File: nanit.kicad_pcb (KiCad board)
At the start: 2 copper layers, 31.2 x 53.3 mm, 66 parts, among them J1 USB_B_Micro, J2 Nokia 2660/2760 mini, Q1 BC857, Q2 IRLML6344, Q4 BC847, SW1 Button 1, SW2 Button 2, U1 LTC4054ES5-4.2, U2 ATmega88PA-AU, Y1 32.768 KHz

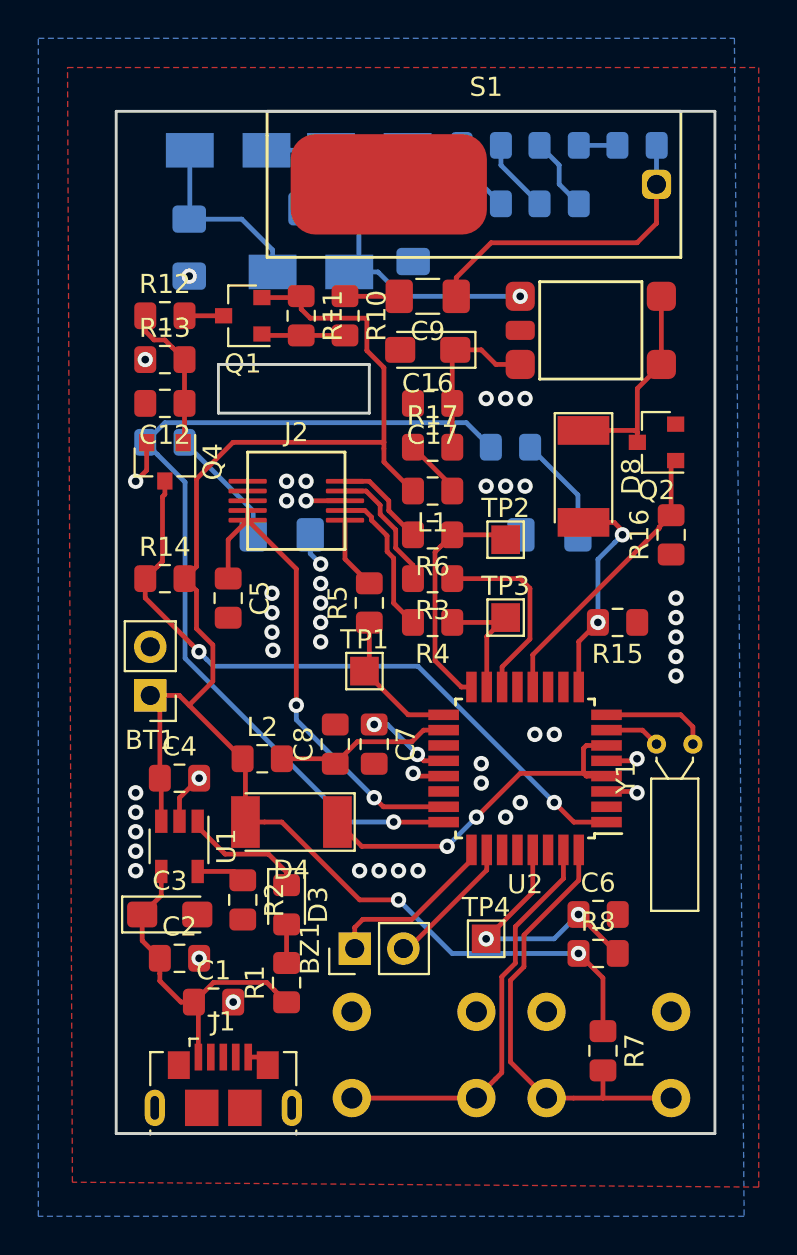
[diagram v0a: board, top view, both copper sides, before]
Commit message: Added LED driver for LCD display, gerbers for rev.A
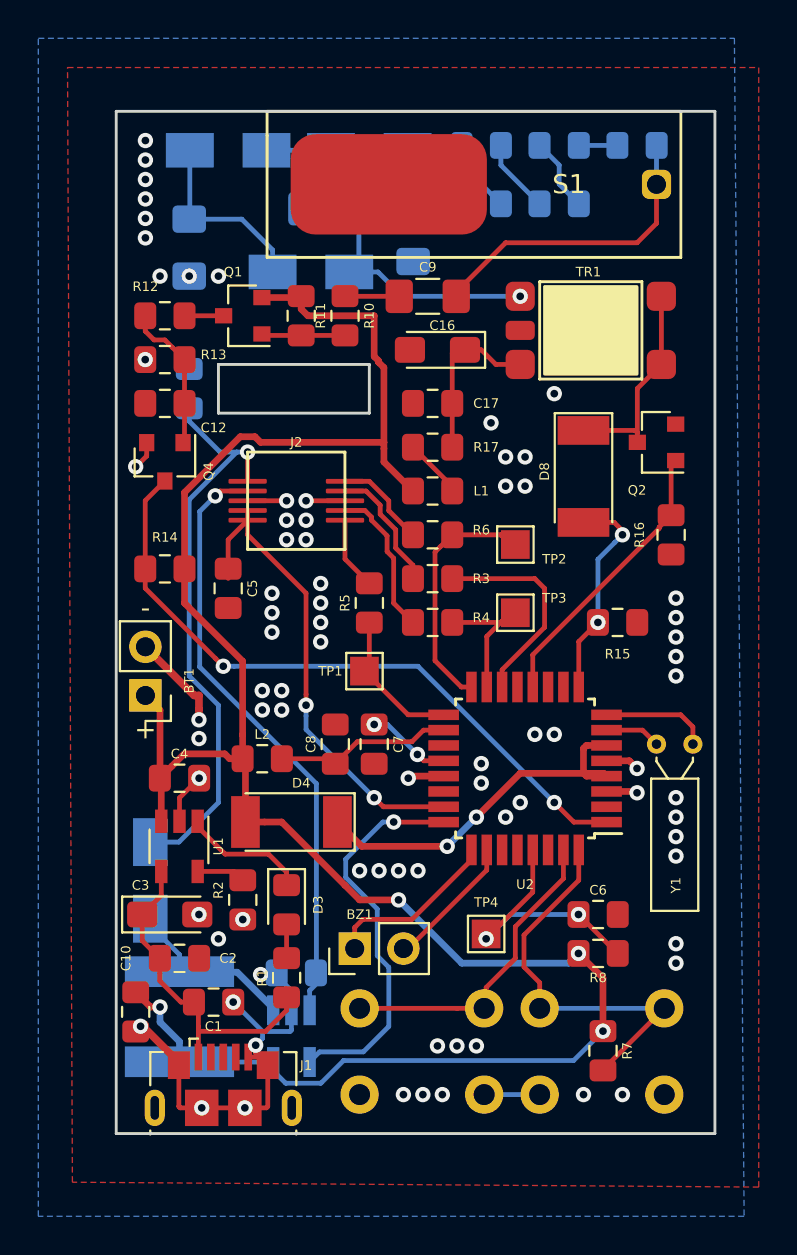
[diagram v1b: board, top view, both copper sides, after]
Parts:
- removed D2: BKL, LED_SMD:LED_1206_3216Metric_Pad1.42x1.75mm_HandSolder
- removed R9-1: 100, Resistor_SMD:R_0805_2012Metric_Pad1.15x1.40mm_HandSolder
- added C10: 1uF, Capacitor_SMD:C_0805_2012Metric_Pad1.15x1.40mm_HandSolder, F.Cu at (115.3, 123.2)
- added C11: 22nF, Capacitor_SMD:C_0805_2012Metric_Pad1.15x1.40mm_HandSolder, B.Cu at (118.1, 90.7)
- added L3: 22uH, Inductor_SMD:L_Bourns-SRN6028, B.Cu at (117.6, 123.4)
- added U3: LT1937, Package_TO_SOT_SMD:SOT-23-5_HandSoldering, B.Cu at (123.4, 124.5)
- D1: value BKL -> SS14; footprint LED_SMD:LED_1206_3216Metric_Pad1.42x1.75mm_HandSolder -> Diode_SMD:D_SMA
- R9: value 100 -> 6.34
- moved R9 28.5 mm to (123.7, 121.2), turned to 180 degrees
- moved D1 19.3 mm to (116.1, 116.3), turned to 270 degrees
- moved SW1 8.10 mm to (136.4, 127.5), turned to 0 degrees
- moved SW2 7.47 mm to (127.0, 127.5), turned to 0 degrees
- moved TP3 0.57 mm to (135.1, 102.4)
- moved TP2 0.57 mm to (135.1, 98.8)
- moved R14 0.51 mm to (116.8, 100.1)
- moved C5 0.51 mm to (120.1, 101.1)
- moved C16 0.51 mm to (131.1, 88.6)
- moved BT1 0.25 mm to (115.8, 106.7)
- moved R1 0.25 mm to (123.2, 121.4)
- moved TP4 0.25 mm to (133.6, 119.1)
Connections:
- D1 pad 1: GNDD -> LCD_BK+
- J2 pad 6: Net-(J2-Pad6) -> LCD_BK+
- J2 pad 7: Net-(J2-Pad7) -> LCD_BK-
- J2 pad 8: Net-(J2-Pad8) -> GNDD
- R9 pad 1: LCD_BK -> LCD_BK-
- R9 pad 2: Net-(D1-Pad2) -> GNDD
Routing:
- net LCD_BK-: track 0.00 -> 32.0 mm, vias 0 -> 1
- net VCC: track 81.3 -> 112.7 mm, vias 2 -> 4
- net LCD_BK+: track 0.00 -> 30.3 mm, vias 0 -> 1
- net GNDD: track 14.8 -> 44.5 mm, vias 48 -> 78
- net LCD_BK: track 48.2 -> 20.4 mm
- net Net-(D2-Pad2): track 5.61 -> 0.00 mm
- net Net-(SW2-Pad2): track 21.3 -> 16.5 mm
- net Net-(R7-Pad2): track 23.1 -> 20.9 mm
- net Net-(D1-Pad2): track 6.31 -> 8.41 mm
- net Net-(R3-Pad1): track 10.0 -> 11.1 mm
- net Net-(C1-Pad1): track 17.4 -> 18.2 mm
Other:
- board text added: "+"
- board text added: "-"
- board text added: "NANIT"
- board text added: "Nokia 2760 LCD"
- board text added: "Warning! High Voltage Parts"
- board text added: "https://github.com/andykarpov/nanit"
- board text added: "rev.A"
